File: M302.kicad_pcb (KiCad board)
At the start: 2 copper layers, 68.6 x 53.3 mm, 26 parts, among them J1 I2C-SHT3x, J2 I2C-ThmCp, J3 I2C-3, J4 I2C-4, J5 I2C-D400, J6 W5500, J7 IM920, J8 PWR+5V, J9 ANALOG-IN, P1 Power, P2 Analog, P3 Digital, P4 Digital, P5 CONN_01X01, P6 CONN_01X01, P7 CONN_01X01, P8 CONN_01X01, SW1 CPU, SW2 D400, SW3 IM920, U1 SFE-BOB-12009

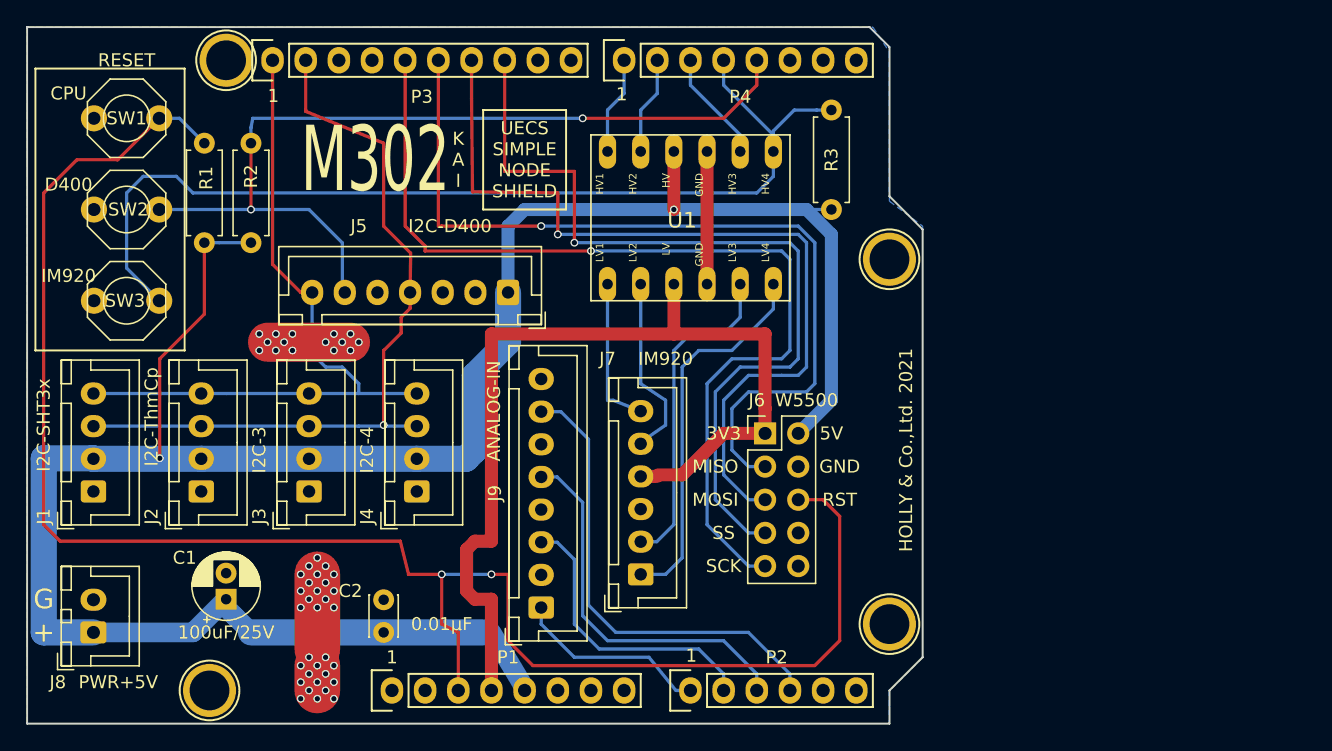
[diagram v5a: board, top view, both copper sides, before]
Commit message: rel: 1.11 コンデンサ3Dモデル変更
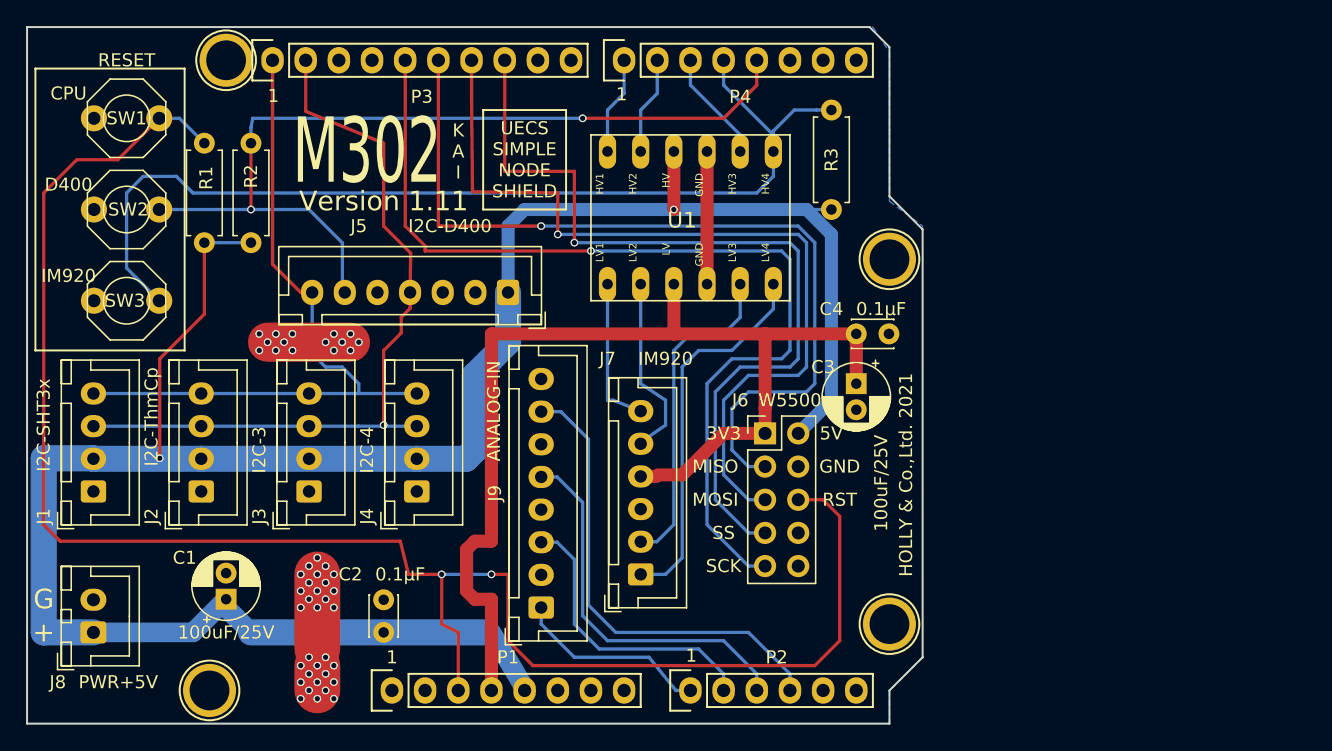
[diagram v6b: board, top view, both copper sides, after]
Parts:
- added C3: 100uF/25V, Capacitor_THT:CP_Radial_D5.0mm_P2.00mm, F.Cu at (174.5, 100.3)
- added C4: 0.1μF, Capacitor_THT:C_Disc_D3.0mm_W2.0mm_P2.50mm, F.Cu at (174.5, 96.5)
- C2: value 0.01μF -> 0.1μF
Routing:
- net +3V3: track 73.6 -> 84.4 mm
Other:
- board text added: "Version 1.11"

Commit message: KiCAD new version
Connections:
- net +3V3 renamed +3.3V
- net /10(**/SS) renamed /10(**/SS)
- net /11(**/MOSI) renamed /11(**/MOSI)
- J5 pad 2: Net-(J5-Pad2) -> unconnected-(J5-Pad2)
- J5 pad 5: Net-(J5-Pad5) -> unconnected-(J5-Pad5)
- J6 pad 10: Net-(J6-Pad10) -> unconnected-(J6-Pad10)
- J6 pad 8: Net-(J6-Pad8) -> unconnected-(J6-Pad8)
- P1 pad 1: Net-(P1-Pad1) -> unconnected-(P1-Pad1)
- P1 pad 8: Net-(P1-Pad8) -> unconnected-(P1-Pad8)
- P2 pad 5: Net-(P2-Pad5) -> unconnected-(P2-Pad5)
- P2 pad 6: Net-(P2-Pad6) -> unconnected-(P2-Pad6)
- P5 pad 1: Net-(P5-Pad1) -> unconnected-(P5-Pad1)
- P6 pad 1: Net-(P6-Pad1) -> unconnected-(P6-Pad1)
- P7 pad 1: Net-(P7-Pad1) -> unconnected-(P7-Pad1)
- P8 pad 1: Net-(P8-Pad1) -> unconnected-(P8-Pad1)
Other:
- net class Default removed
- board text added: "HOLLY & Co.,Ltd. 2022"
- board text added: "Version 1.12"
- board text removed: "HOLLY & Co.,Ltd. 2021"
- board text removed: "Version 1.11"
